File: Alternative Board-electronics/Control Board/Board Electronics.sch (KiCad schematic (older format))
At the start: 13 parts, among them J1 CONN_01X06, J2 CONN_01X05, J3 CONN_02X12, SW1 SW_SPDT_LED, U1 Adafruit_Bluefruit_LE_UART_Fr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, U2 Powerboost1000C, U3 MCP23017, U4 MCP23017, U5 MCP23017

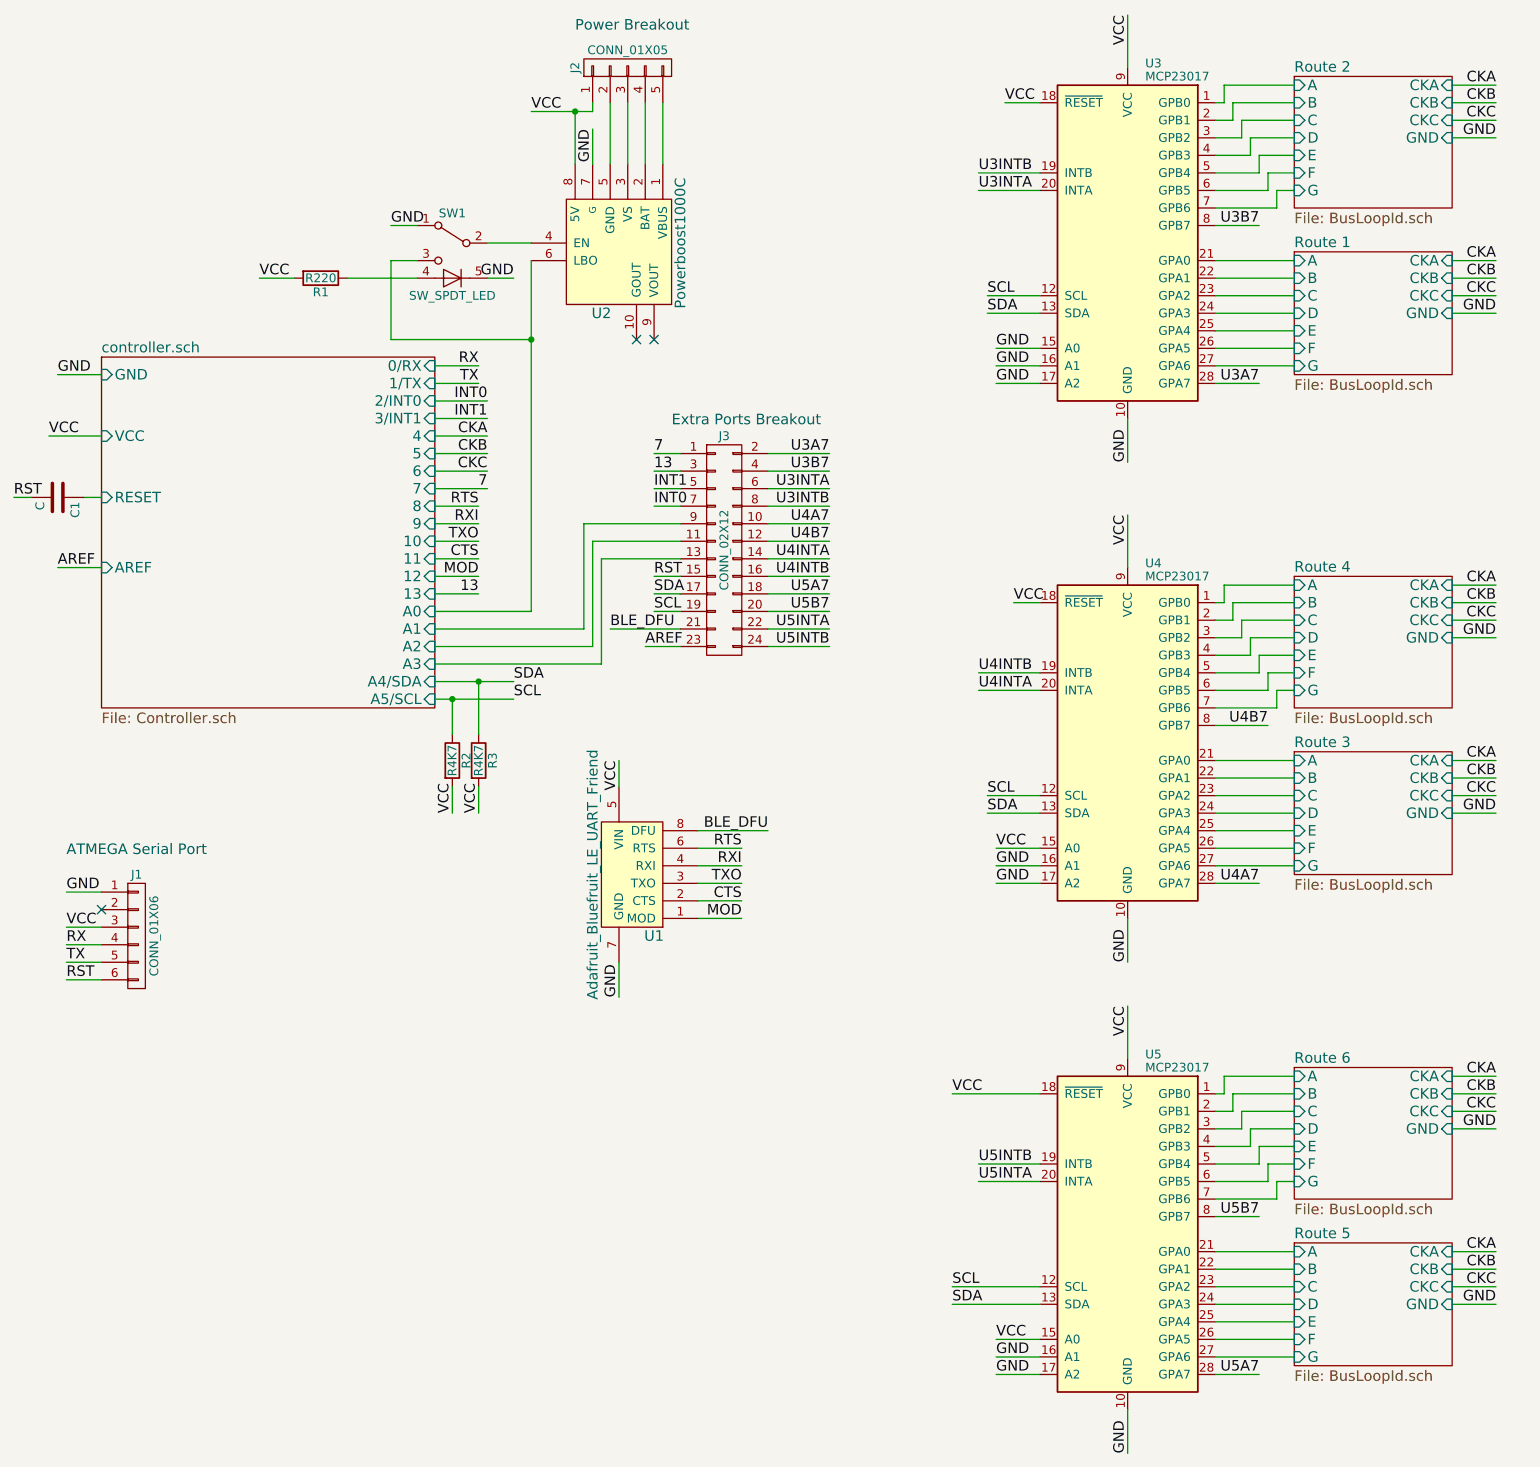
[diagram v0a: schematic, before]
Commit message: update Kicad files to have new schematic design
This new schematic design is nested under a new folder called
alternative board electronics. It breaks apart the control circuitry and
the led attachment points to save PCB space (and this cost).

This may become the default schematics in a future revision, and the
all-in-one board will become the alternative.
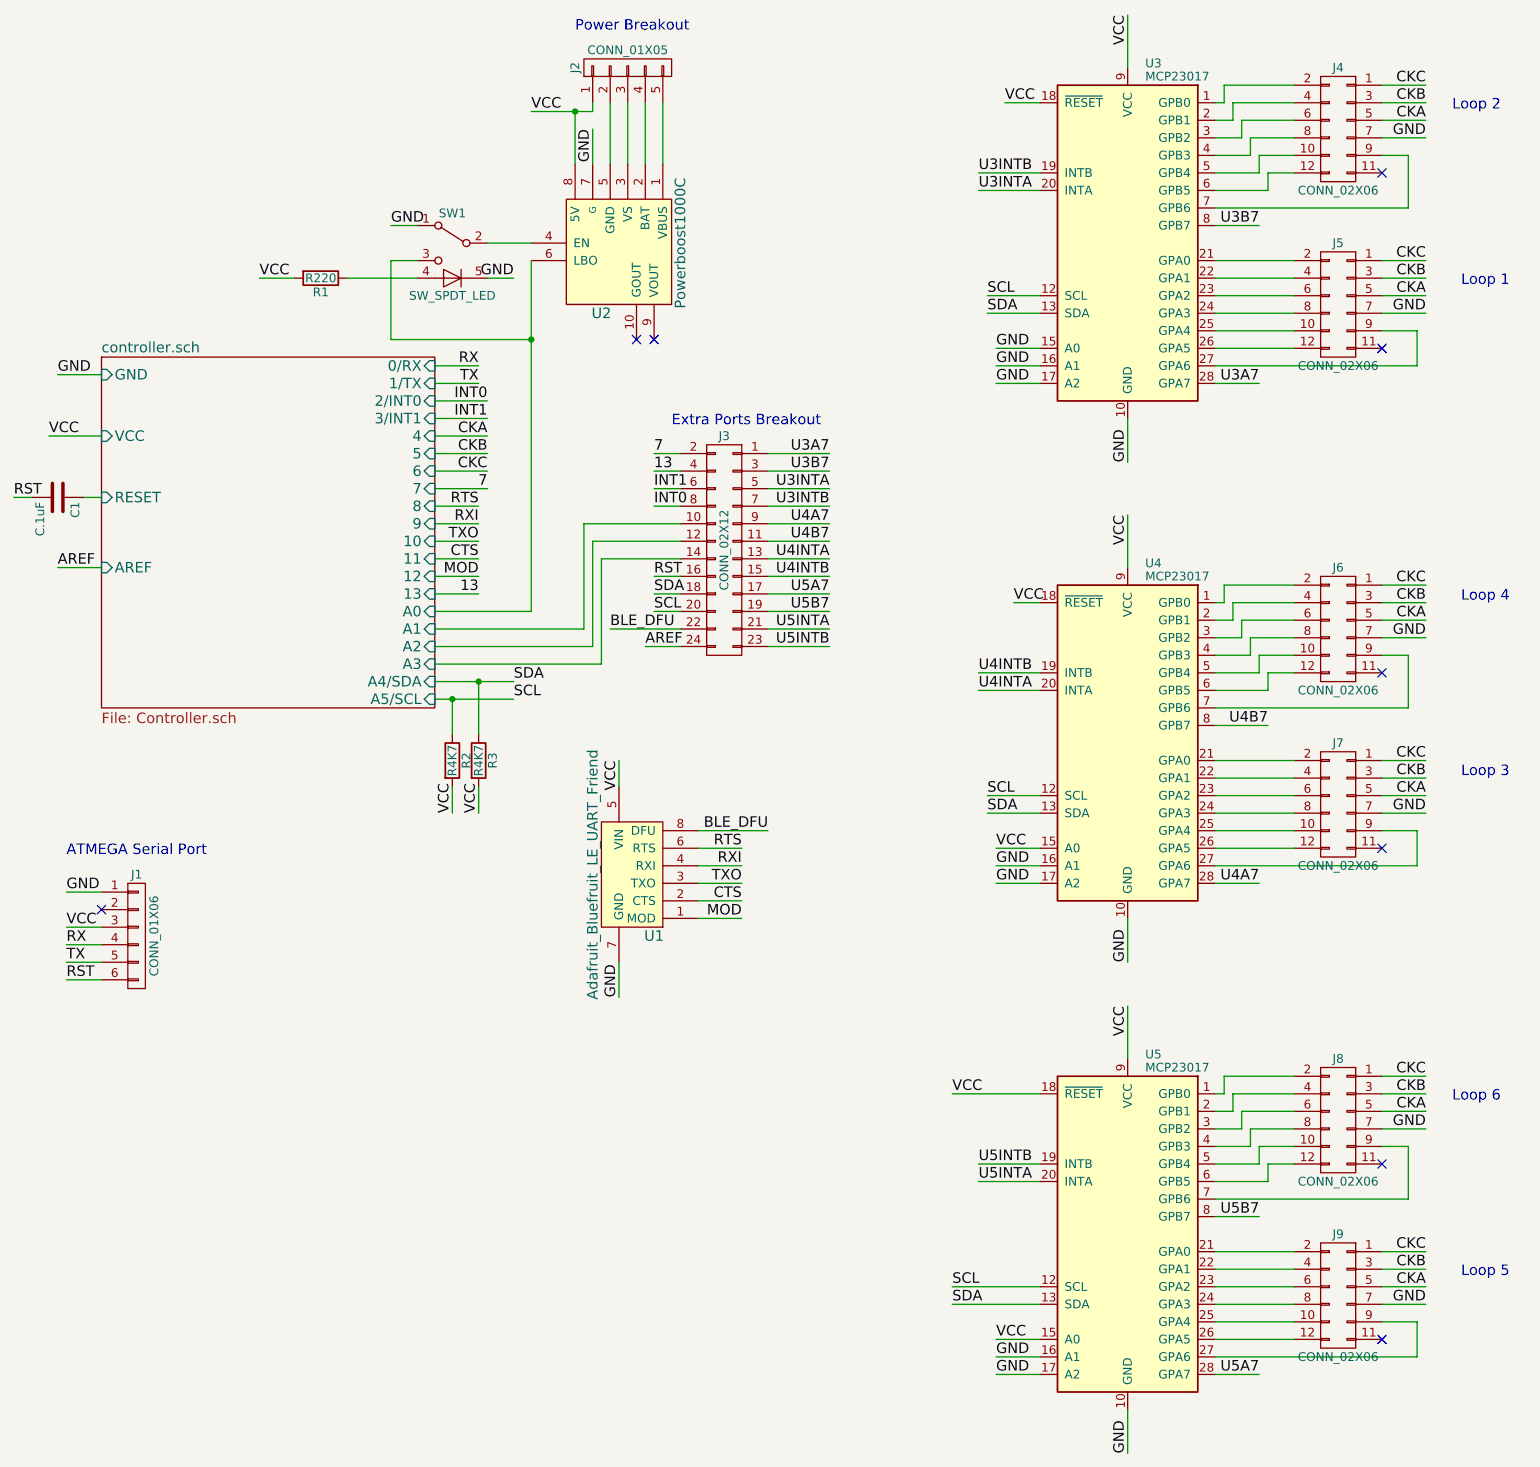
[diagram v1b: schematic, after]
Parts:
- added J4, J5, J6, J7, J8, J9: CONN_02X06, Pin_Headers:Pin_Header_Straight_2x06_Pitch2.54mm, symbol CONN_02X06
- C1: value C -> C.1uF
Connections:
- net 13: now also J3.4 (P4); no longer J3.3 (P3)
- net 7: now also J3.2 (P2); no longer J3.1 (P1)
- net AREF: now also J3.24 (P24); no longer J3.23 (P23)
- net BLE_DFU: now also J3.22 (P22); no longer J3.21 (P21)
- net CKA: now also J4.5 (P5), J5.5 (P5), J6.5 (P5), J7.5 (P5), J8.5 (P5), J9.5 (P5)
- net CKB: now also J4.3 (P3), J5.3 (P3), J6.3 (P3), J7.3 (P3), J8.3 (P3), J9.3 (P3)
- net CKC: now also J4.1 (P1), J5.1 (P1), J6.1 (P1), J7.1 (P1), J8.1 (P1), J9.1 (P1)
- net GND: now also J4.7 (P7), J5.7 (P7), J6.7 (P7), J7.7 (P7), J8.7 (P7), J9.7 (P7)
- net INT0: now also J3.8 (P8); no longer J3.7 (P7)
- net INT1: now also J3.6 (P6); no longer J3.5 (P5)
- net RST: now also J3.16 (P16); no longer J3.15 (P15)
- net SCL: now also J3.20 (P20); no longer J3.19 (P19)
- net SDA: now also J3.18 (P18); no longer J3.17 (P17)
- net U3A7: now also J3.1 (P1); no longer J3.2 (P2)
- net U3B7: now also J3.3 (P3); no longer J3.4 (P4)
- net U3INTA: now also J3.5 (P5); no longer J3.6 (P6)
- net U3INTB: now also J3.7 (P7); no longer J3.8 (P8)
- net U4A7: now also J3.9 (P9); no longer J3.10 (P10)
- net U4B7: now also J3.11 (P11); no longer J3.12 (P12)
- net U4INTA: now also J3.13 (P13); no longer J3.14 (P14)
- net U4INTB: now also J3.15 (P15); no longer J3.16 (P16)
- net U5A7: now also J3.17 (P17); no longer J3.18 (P18)
- net U5B7: now also J3.19 (P19); no longer J3.20 (P20)
- net U5INTA: now also J3.21 (P21); no longer J3.22 (P22)
- net U5INTB: now also J3.23 (P23); no longer J3.24 (P24)
- net controller.sch/A1: now also J3.10 (P10); no longer J3.9 (P9)
- net controller.sch/A2: now also J3.12 (P12); no longer J3.11 (P11)
- net controller.sch/A3: now also J3.14 (P14); no longer J3.13 (P13)
- net Route 1/A: no longer names the net of U3.21 (GPA0)
- net Route 1/A: now also J5.2 (P2)
- net Route 1/B: no longer names the net of U3.22 (GPA1)
- net Route 1/B: now also J5.4 (P4)
- net Route 1/C: no longer names the net of U3.23 (GPA2)
- net Route 1/C: now also J5.6 (P6)
- net Route 1/D: no longer names the net of U3.24 (GPA3)
- net Route 1/D: now also J5.8 (P8)
- net Route 1/E: no longer names the net of U3.25 (GPA4)
- net Route 1/E: now also J5.10 (P10)
- net Route 1/F: no longer names the net of U3.26 (GPA5)
- net Route 1/F: now also J5.12 (P12)
- net Route 1/G: no longer names the net of U3.27 (GPA6)
- net Route 1/G: now also J5.9 (P9)
- net Route 2/A: no longer names the net of U3.1 (GPB0)
- net Route 2/A: now also J4.2 (P2)
- net Route 2/B: no longer names the net of U3.2 (GPB1)
- net Route 2/B: now also J4.4 (P4)
- net Route 2/C: no longer names the net of U3.3 (GPB2)
- net Route 2/C: now also J4.6 (P6)
- net Route 2/D: no longer names the net of U3.4 (GPB3)
- net Route 2/D: now also J4.8 (P8)
- net Route 2/E: no longer names the net of U3.5 (GPB4)
- net Route 2/E: now also J4.10 (P10)
- net Route 2/F: no longer names the net of U3.6 (GPB5)
- net Route 2/F: now also J4.12 (P12)
- net Route 2/G: no longer names the net of U3.7 (GPB6)
- net Route 2/G: now also J4.9 (P9)
- net Route 3/A: no longer names the net of U4.21 (GPA0)
- net Route 3/A: now also J7.2 (P2)
- net Route 3/B: no longer names the net of U4.22 (GPA1)
- net Route 3/B: now also J7.4 (P4)
- net Route 3/C: no longer names the net of U4.23 (GPA2)
- net Route 3/C: now also J7.6 (P6)
- net Route 3/D: no longer names the net of U4.24 (GPA3)
- net Route 3/D: now also J7.8 (P8)
- net Route 3/E: no longer names the net of U4.25 (GPA4)
- net Route 3/E: now also J7.10 (P10)
- net Route 3/F: no longer names the net of U4.26 (GPA5)
- net Route 3/F: now also J7.12 (P12)
- net Route 3/G: no longer names the net of U4.27 (GPA6)
- net Route 3/G: now also J7.9 (P9)
- net Route 4/A: no longer names the net of U4.1 (GPB0)
- net Route 4/A: now also J6.2 (P2)
- net Route 4/B: no longer names the net of U4.2 (GPB1)
- net Route 4/B: now also J6.4 (P4)
- net Route 4/C: no longer names the net of U4.3 (GPB2)
- net Route 4/C: now also J6.6 (P6)
- net Route 4/D: no longer names the net of U4.4 (GPB3)
- net Route 4/D: now also J6.8 (P8)
- net Route 4/E: no longer names the net of U4.5 (GPB4)
- net Route 4/E: now also J6.10 (P10)
- net Route 4/F: no longer names the net of U4.6 (GPB5)
- net Route 4/F: now also J6.12 (P12)
- net Route 4/G: no longer names the net of U4.7 (GPB6)
- net Route 4/G: now also J6.9 (P9)
- net Route 5/A: no longer names the net of U5.21 (GPA0)
- net Route 5/A: now also J9.2 (P2)
- net Route 5/B: no longer names the net of U5.22 (GPA1)
- net Route 5/B: now also J9.4 (P4)
- net Route 5/C: no longer names the net of U5.23 (GPA2)
- net Route 5/C: now also J9.6 (P6)
- net Route 5/D: no longer names the net of U5.24 (GPA3)
- net Route 5/D: now also J9.8 (P8)
- net Route 5/E: no longer names the net of U5.25 (GPA4)
- net Route 5/E: now also J9.10 (P10)
- net Route 5/F: no longer names the net of U5.26 (GPA5)
- net Route 5/F: now also J9.12 (P12)
- net Route 5/G: no longer names the net of U5.27 (GPA6)
- net Route 5/G: now also J9.9 (P9)
- net Route 6/A: no longer names the net of U5.1 (GPB0)
- net Route 6/A: now also J8.2 (P2)
- net Route 6/B: no longer names the net of U5.2 (GPB1)
- net Route 6/B: now also J8.4 (P4)
- net Route 6/C: no longer names the net of U5.3 (GPB2)
- net Route 6/C: now also J8.6 (P6)
- net Route 6/D: no longer names the net of U5.4 (GPB3)
- net Route 6/D: now also J8.8 (P8)
- net Route 6/E: no longer names the net of U5.5 (GPB4)
- net Route 6/E: now also J8.10 (P10)
- net Route 6/F: no longer names the net of U5.6 (GPB5)
- net Route 6/F: now also J8.12 (P12)
- net Route 6/G: no longer names the net of U5.7 (GPB6)
- net Route 6/G: now also J8.9 (P9)
- no-connect marks 3 -> 9
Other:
- note added: "Loop 1\n"
- note added: "Loop 2"
- note added: "Loop 3"
- note added: "Loop 4"
- note added: "Loop 5"
- note added: "Loop 6"
